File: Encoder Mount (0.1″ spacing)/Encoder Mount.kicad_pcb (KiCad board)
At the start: 2 copper layers, 23 x 16 mm, 9 parts, among them J1 Conn_01x03_Pin, J2 Conn_01x03_Pin

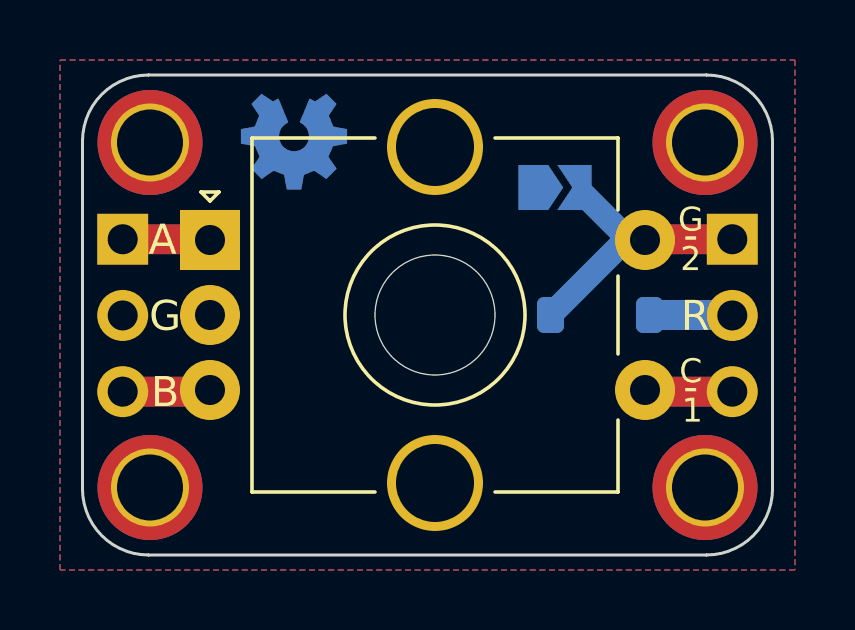
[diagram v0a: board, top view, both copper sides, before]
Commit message: Add JLC order number locator
See [“ How to remove order number from your PCB?”](https://jlcpcb.com/help/article/50-How-to-remove-order-number-from-your-PCB)
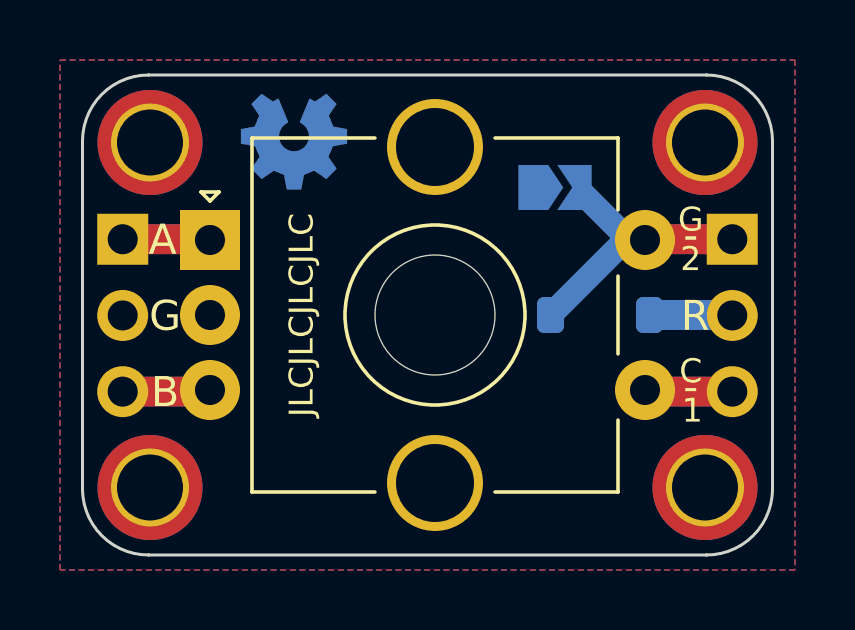
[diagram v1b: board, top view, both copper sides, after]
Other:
- board text added: "JLCJLCJLCJLC"
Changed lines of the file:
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@@
     (effects (font (size 0.8 0.8) (thickness 0.15)) (justify bottom))
+  )
+  (gr_text "JLCJLCJLCJLC" (at 95.55 99.999999 90) (layer "F.SilkS")
+    (effects (font (size 0.8 0.8) (thickness 0.15)))
   )
   (gr_text "-" (at 108.525 102.4025) (layer "F.SilkS")
